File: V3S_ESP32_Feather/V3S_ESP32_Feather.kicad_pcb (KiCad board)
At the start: 2 copper layers, 30.5 x 49.5 mm, 82 parts, among them J1 USB_Micro, J10 UART, J2 PWM, J3 CAM, J4 I2C, J5 U.FL-R-SMT(01), J7 Micro_SD_Card_Det, J9 I2C, U1 V3S, U2 ADP322ACPZ-145-R7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

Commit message: Apply V3s design guide recommendations
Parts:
- added R12: 33R, Resistor_SMD:R_0201_0603Metric, F.Cu at (51.9, 56.6)
- added R17: 33R, Resistor_SMD:R_0201_0603Metric, B.Cu at (37.7, 61.8)
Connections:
- J3 pad 13: /All V3s input output/CSI_MCLK -> Net-(J3-Pad13)
- U1 pad 105: /All V3s input output/PF2 -> Net-(R12-Pad2)
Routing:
- net /All V3s input output/PF2: track 43.8 -> 24.3 mm, vias 1 -> 0
- net Net-(R12-Pad2): track 0.00 -> 19.0 mm, vias 0 -> 1
- net /All V3s input output/CSI_MCLK: track 23.2 -> 19.1 mm
- net Net-(J3-Pad13): track 0.00 -> 3.93 mm

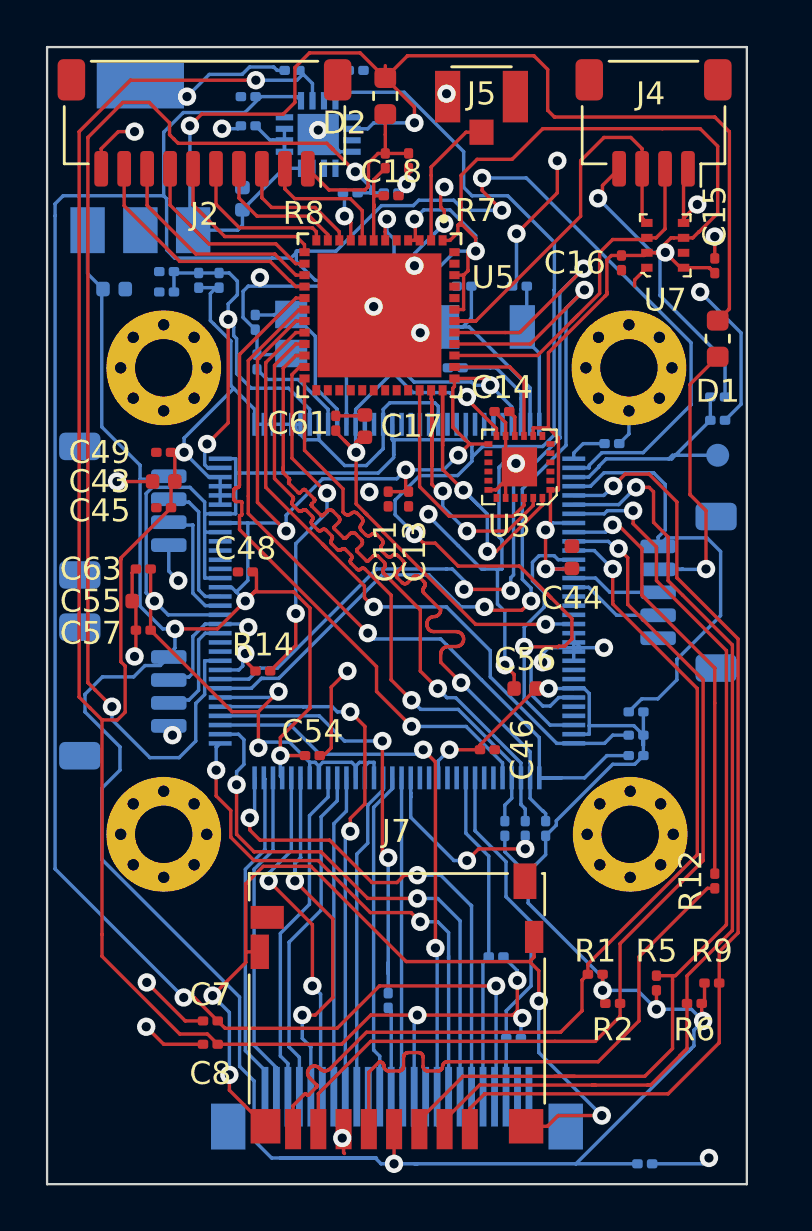
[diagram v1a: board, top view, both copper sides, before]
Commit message: Move via from pad and rebuild fab files
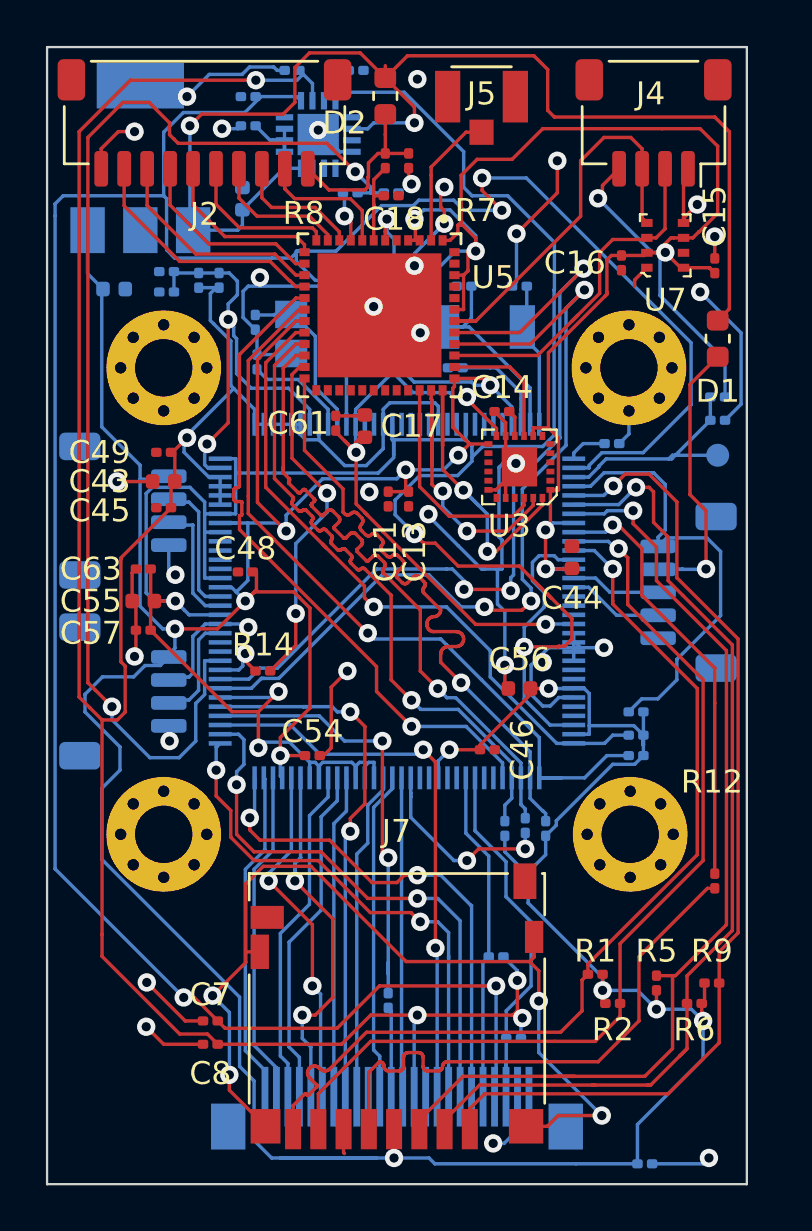
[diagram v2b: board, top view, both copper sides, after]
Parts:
- C1, C15, C16, C48, C49, C54, C61, C63, C64, C65: value 100nF -> 0.1uF
- C11: value 10nF -> 1uF
- moved C56 0.25 mm to (43.4, 48.3)
- moved R15 0.13 mm to (43.7, 54.2)
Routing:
- net GND: track 109.2 -> 112.4 mm
- net +3V3: track 261.9 -> 260.6 mm
- net +1V2: track 114.4 -> 115.3 mm
- net +1V8: track 117.9 -> 118.4 mm

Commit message: increased power track, increased version to 0.2 and re build fab files
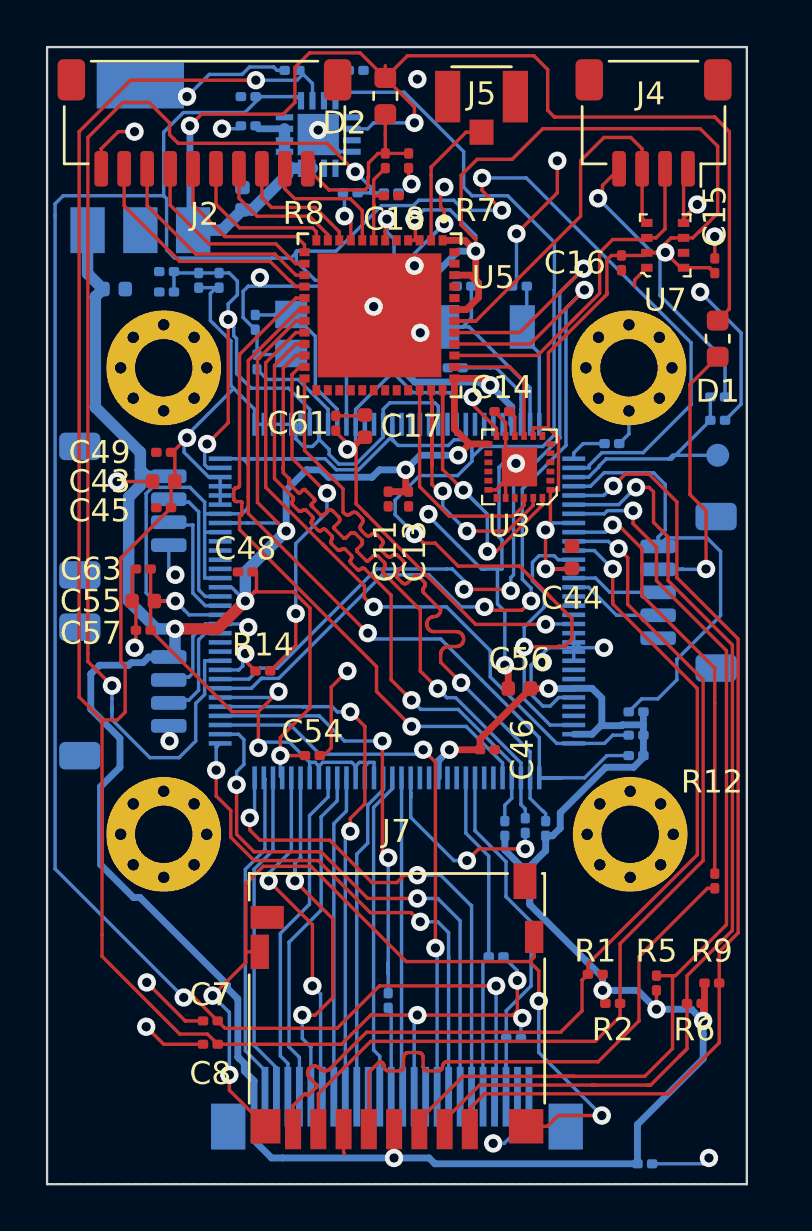
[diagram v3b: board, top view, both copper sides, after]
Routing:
- net +3V3: track 260.6 -> 284.1 mm
- net +1V2: track 115.3 -> 118.7 mm
- net +1V8: track 118.4 -> 119.6 mm
- net +3V0: track 142.2 -> 143.1 mm
- net /PMIC Power Battery/VIN: track 58.7 -> 59.3 mm
- net GND: track 112.4 -> 112.1 mm, vias 32 -> 31
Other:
- board text added: "SmartBridgeMicro V0.2 By Crylog"
- board text removed: "SmartBridgeMicro V0.1 By Crylog"

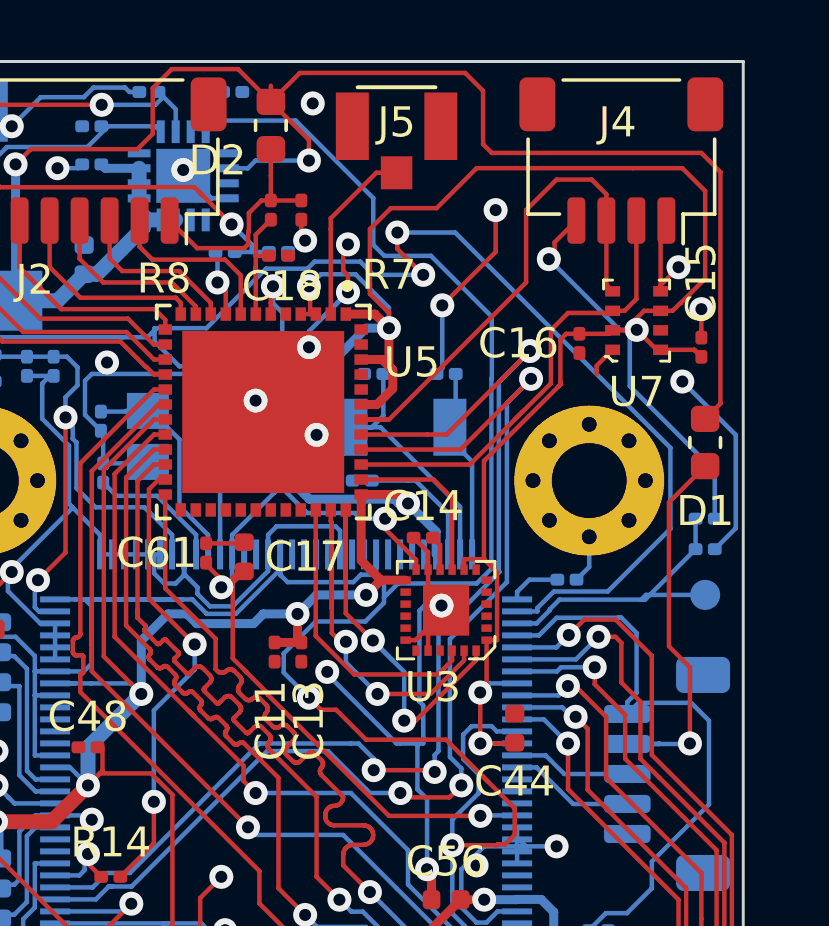
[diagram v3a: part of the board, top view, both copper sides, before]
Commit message: fix d1, d2 package
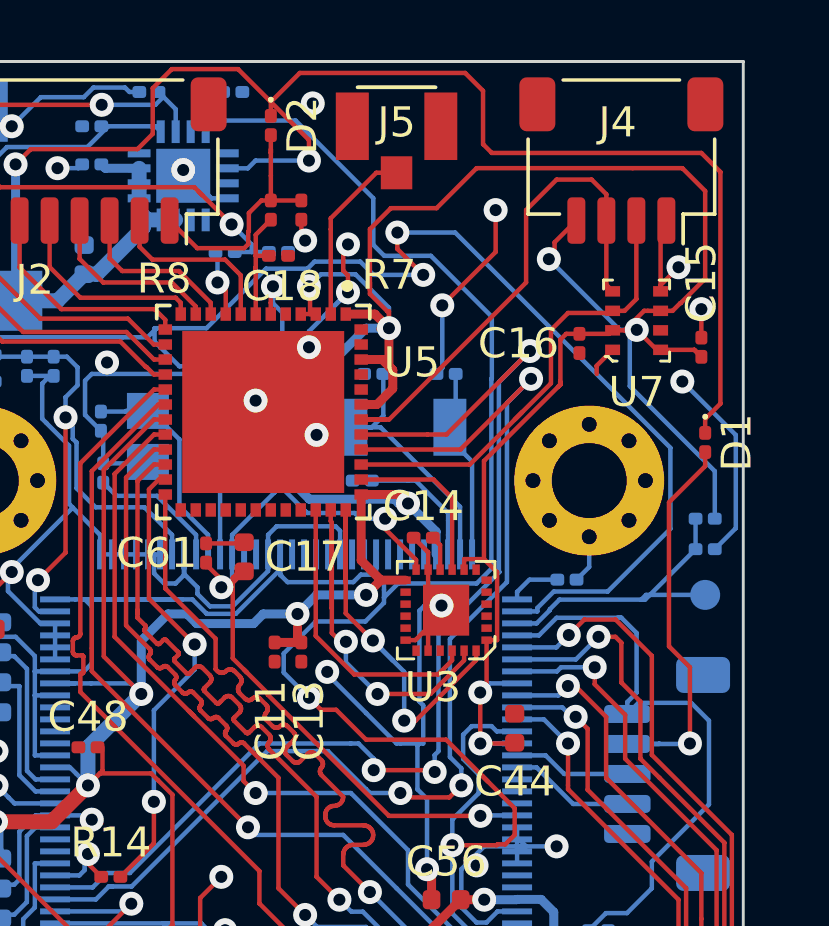
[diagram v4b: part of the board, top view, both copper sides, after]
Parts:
- D1, D2: footprint Resistor_SMD:R_0603_1608Metric -> Diode_SMD:D_0201_0603Metric
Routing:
- net +BATT: track 7.74 -> 8.33 mm

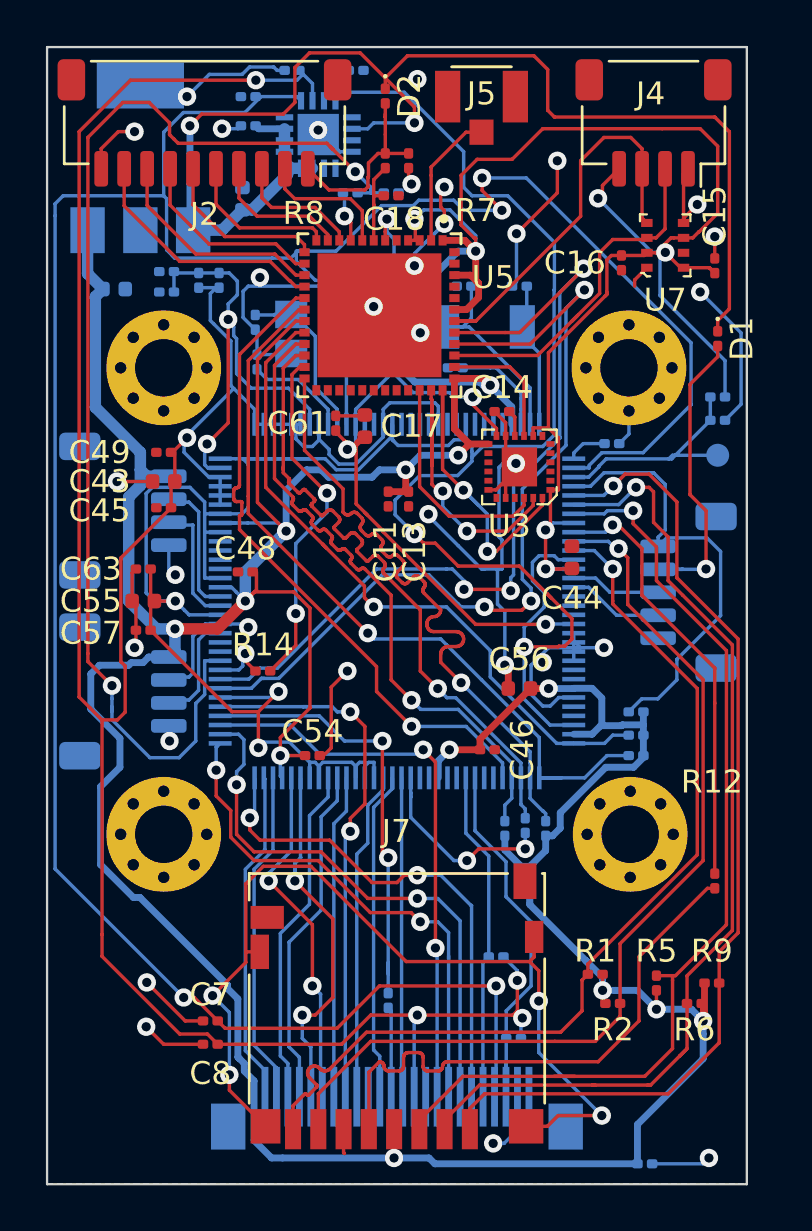
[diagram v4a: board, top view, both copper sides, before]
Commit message: fix component packages
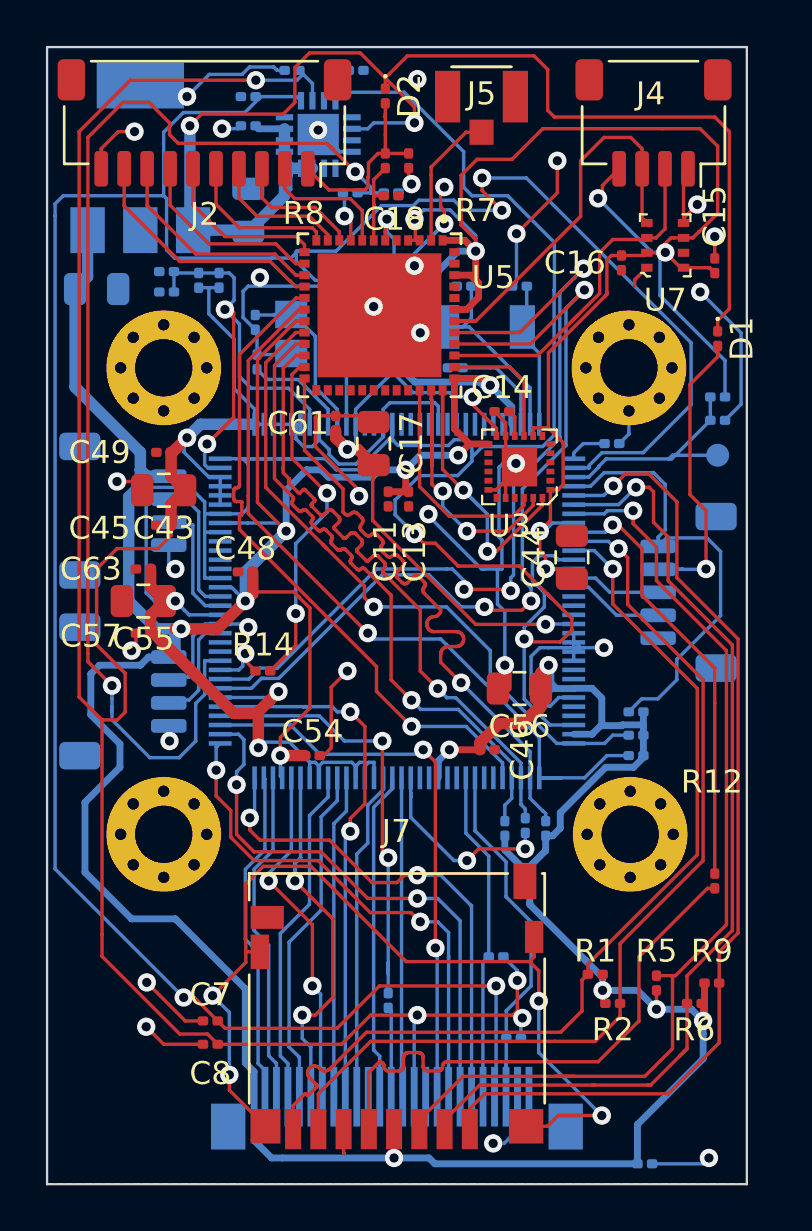
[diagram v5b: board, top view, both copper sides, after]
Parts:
- C17, C43, C44, C5, C55, C56, C9: footprint Capacitor_SMD:C_0402_1005Metric -> Capacitor_SMD:C_0805_2012Metric
- moved C17 0.85 mm to (37.1, 37.6)
- moved C45 0.76 mm to (27.9, 41.1)
- moved C9 0.76 mm to (25.0, 30.9)
- moved C5 0.57 mm to (31.6, 27.4)
- moved C43 0.38 mm to (27.9, 39.6)
- moved C57 0.13 mm to (27.1, 45.8)
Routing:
- net /PMIC Power Battery/VIN: track 59.7 -> 69.8 mm
- net +3V3: track 284.1 -> 293.1 mm
- net +1V2: track 118.7 -> 122.8 mm
- net +1V8: track 119.6 -> 123.3 mm
- net GND: track 112.1 -> 114.6 mm
- net /PMIC Power Battery/SVREF: track 20.0 -> 22.2 mm
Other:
- net class Default: clearance 0.1 -> 0.08
- net class Power added: clearance 0.08, trace_width 0.5, via_dia 0.8, via_drill 0.4
- rule trace_clearance: 0.1 -> 0.08
